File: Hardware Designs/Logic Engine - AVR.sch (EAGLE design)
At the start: 39 parts, among them IC1 MEGA328P, U1 LP2985, U2 HEX_CONVERTER, Y1 16MHz

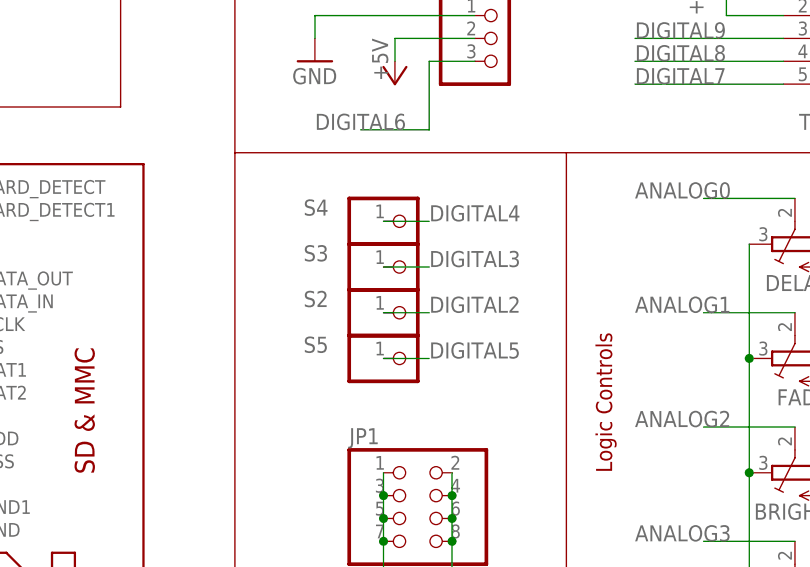
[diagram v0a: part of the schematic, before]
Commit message: Updated AVR board to production version
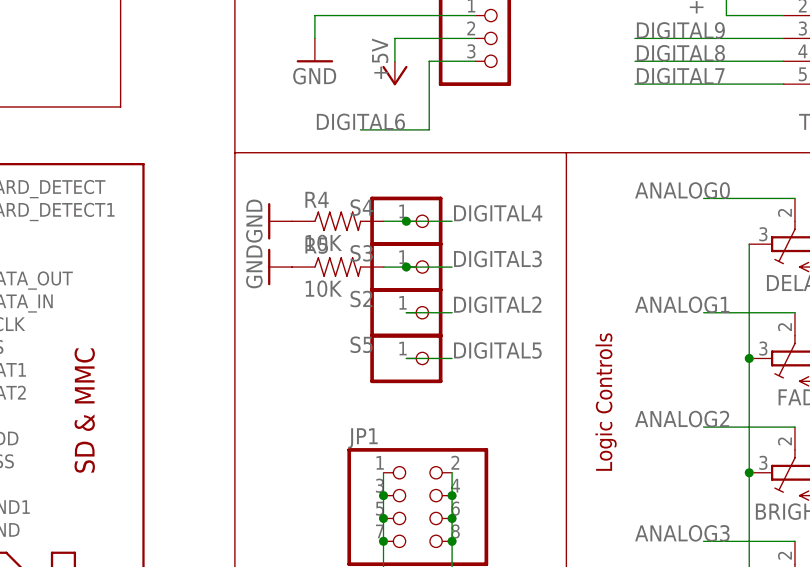
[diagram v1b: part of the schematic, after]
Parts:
- added R4, R5: 10K, SparkFun-Resistors:RESISTOR0603
- FTDI: value GRN TX RX 5V G BLK -> GRN TX RX 5V G BLK
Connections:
- net DIGITAL3: now also R5.2
- net DIGITAL4: now also R4.2
- net GND: now also R4.1, R5.1
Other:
- moved on the sheet: S2, S3, S4, S5
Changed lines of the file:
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@@
 <part name="GND11" library="supply1" deviceset="GND" device=""/>
 <part name="GND12" library="supply1" deviceset="GND" device=""/>
-<part name="FTDI" library="carduino" deviceset="PINHD-1X6" device="CLEAN" value="GRN  TX RX  5V   G  BLK"/>
+<part name="FTDI" library="carduino" deviceset="PINHD-1X6" device="CLEAN" value="GRN TX RX 5V G BLK"/>
 <part name="FRAME1" library="frames" deviceset="LETTER_L" device=""/>
 <part name="I2C" library="carduino" deviceset="PINHD-1X4" device="CB"/>
@@
 <part name="C5" library="adafruit" deviceset="CPOL-US" device="D" value="100uF"/>
 <part name="C6" library="adafruit" deviceset="C-US" device="C0805K" value="10uF"/>
+<part name="R4" library="SparkFun-Resistors" deviceset="RESISTOR" device="0603" value="10K"/>
+<part name="R5" library="SparkFun-Resistors" deviceset="RESISTOR" device="0603" value="10K"/>
+<part name="GND13" library="supply1" deviceset="GND" device=""/>
+<part name="GND14" library="supply1" deviceset="GND" device=""/>
 </parts>
 <sheets>
@@
 <instance part="R8" gate="G$1" x="106.68" y="160.02" rot="R270"/>
 <instance part="JP1" gate="A" x="190.5" y="83.82"/>
-<instance part="S4" gate="G$1" x="190.5" y="116.84" smashed="yes">
-<attribute name="NAME" x="179.07" y="117.475" size="1.778" layer="95"/>
-<attribute name="VALUE" x="184.15" y="111.76" size="1.778" layer="96"/>
-</instance>
-<instance part="S3" gate="G$1" x="190.5" y="111.76" smashed="yes">
-<attribute name="NAME" x="179.07" y="112.395" size="1.778" layer="95"/>
-<attribute name="VALUE" x="184.15" y="106.68" size="1.778" layer="96"/>
-</instance>
-<instance part="S2" gate="G$1" x="190.5" y="106.68" smashed="yes">
-<attribute name="NAME" x="179.07" y="107.315" size="1.778" layer="95"/>
-<attribute name="VALUE" x="184.15" y="101.6" size="1.778" layer="96"/>
-</instance>
-<instance part="S5" gate="G$1" x="190.5" y="101.6" smashed="yes">
-<attribute name="NAME" x="179.07" y="102.235" size="1.778" layer="95"/>
-<attribute name="VALUE" x="184.15" y="96.52" size="1.778" layer="96"/>
+<instance part="S4" gate="G$1" x="193.04" y="116.84" smashed="yes">
+<attribute name="NAME" x="184.15" y="117.475" size="1.778" layer="95"/>
+<attribute name="VALUE" x="186.69" y="111.76" size="1.778" layer="96"/>
+</instance>
+<instance part="S3" gate="G$1" x="193.04" y="111.76" smashed="yes">
+<attribute name="NAME" x="184.15" y="112.395" size="1.778" layer="95"/>
+<attribute name="VALUE" x="186.69" y="106.68" size="1.778" layer="96"/>
+</instance>
+<instance part="S2" gate="G$1" x="193.04" y="106.68" smashed="yes">
+<attribute name="NAME" x="184.15" y="107.315" size="1.778" layer="95"/>
+<attribute name="VALUE" x="186.69" y="101.6" size="1.778" layer="96"/>
+</instance>
+<instance part="S5" gate="G$1" x="193.04" y="101.6" smashed="yes">
+<attribute name="NAME" x="184.15" y="102.235" size="1.778" layer="95"/>
+<attribute name="VALUE" x="186.69" y="96.52" size="1.778" layer="96"/>
 </instance>
 <instance part="GND16" gate="1" x="195.58" y="73.66"/>
@@
 <instance part="C5" gate="G$1" x="53.34" y="165.1"/>
 <instance part="C6" gate="G$1" x="78.74" y="93.98"/>
+<instance part="R4" gate="G$1" x="182.88" y="116.84"/>
+<instance part="R5" gate="G$1" x="182.88" y="111.76"/>
+<instance part="GND13" gate="1" x="175.26" y="116.84" rot="R270"/>
+<instance part="GND14" gate="1" x="175.26" y="111.76" rot="R270"/>
 </instances>
 <busses>
@@
 <pinref part="C6" gate="G$1" pin="2"/>
 </segment>
+<segment>
+<pinref part="R4" gate="G$1" pin="1"/>
+<pinref part="GND13" gate="1" pin="GND"/>
+</segment>
+<segment>
+<pinref part="R5" gate="G$1" pin="1"/>
+<pinref part="GND14" gate="1" pin="GND"/>
+</segment>
 </net>
 <net name="N$1" class="0">
@@
 </segment>
 <segment>
-<label x="193.04" y="101.6" size="1.778" layer="95"/>
+<label x="195.58" y="101.6" size="1.778" layer="95"/>
 <pinref part="S5" gate="G$1" pin="1"/>
-<wire x1="187.96" y1="101.6" x2="193.04" y2="101.6" width="0.1524" layer="91"/>
+<wire x1="190.5" y1="101.6" x2="195.58" y2="101.6" width="0.1524" layer="91"/>
 </segment>
 </net>
@@
 </segment>
 <segment>
-<label x="193.04" y="116.84" size="1.778" layer="95"/>
+<label x="195.58" y="116.84" size="1.778" layer="95"/>
 <pinref part="S4" gate="G$1" pin="1"/>
-<wire x1="187.96" y1="116.84" x2="193.04" y2="116.84" width="0.1524" layer="91"/>
+<wire x1="190.5" y1="116.84" x2="195.58" y2="116.84" width="0.1524" layer="91"/>
+<pinref part="R4" gate="G$1" pin="2"/>
+<wire x1="187.96" y1="116.84" x2="190.5" y2="116.84" width="0.1524" layer="91"/>
+<junction x="190.5" y="116.84"/>
 </segment>
 </net>
@@
 </segment>
 <segment>
-<label x="193.04" y="111.76" size="1.778" layer="95"/>
+<label x="195.58" y="111.76" size="1.778" layer="95"/>
 <pinref part="S3" gate="G$1" pin="1"/>
-<wire x1="187.96" y1="111.76" x2="193.04" y2="111.76" width="0.1524" layer="91"/>
+<wire x1="190.5" y1="111.76" x2="195.58" y2="111.76" width="0.1524" layer="91"/>
+<pinref part="R5" gate="G$1" pin="2"/>
+<wire x1="187.96" y1="111.76" x2="190.5" y2="111.76" width="0.1524" layer="91"/>
+<junction x="190.5" y="111.76"/>
 </segment>
 </net>
@@
 </segment>
 <segment>
-<label x="193.04" y="106.68" size="1.778" layer="95"/>
+<label x="195.58" y="106.68" size="1.778" layer="95"/>
 <pinref part="S2" gate="G$1" pin="1"/>
-<wire x1="187.96" y1="106.68" x2="193.04" y2="106.68" width="0.1524" layer="91"/>
-</segment>
-</net>
+<wire x1="190.5" y1="106.68" x2="195.58" y2="106.68" width="0.1524" layer="91"/>
+</segment>
+</net>

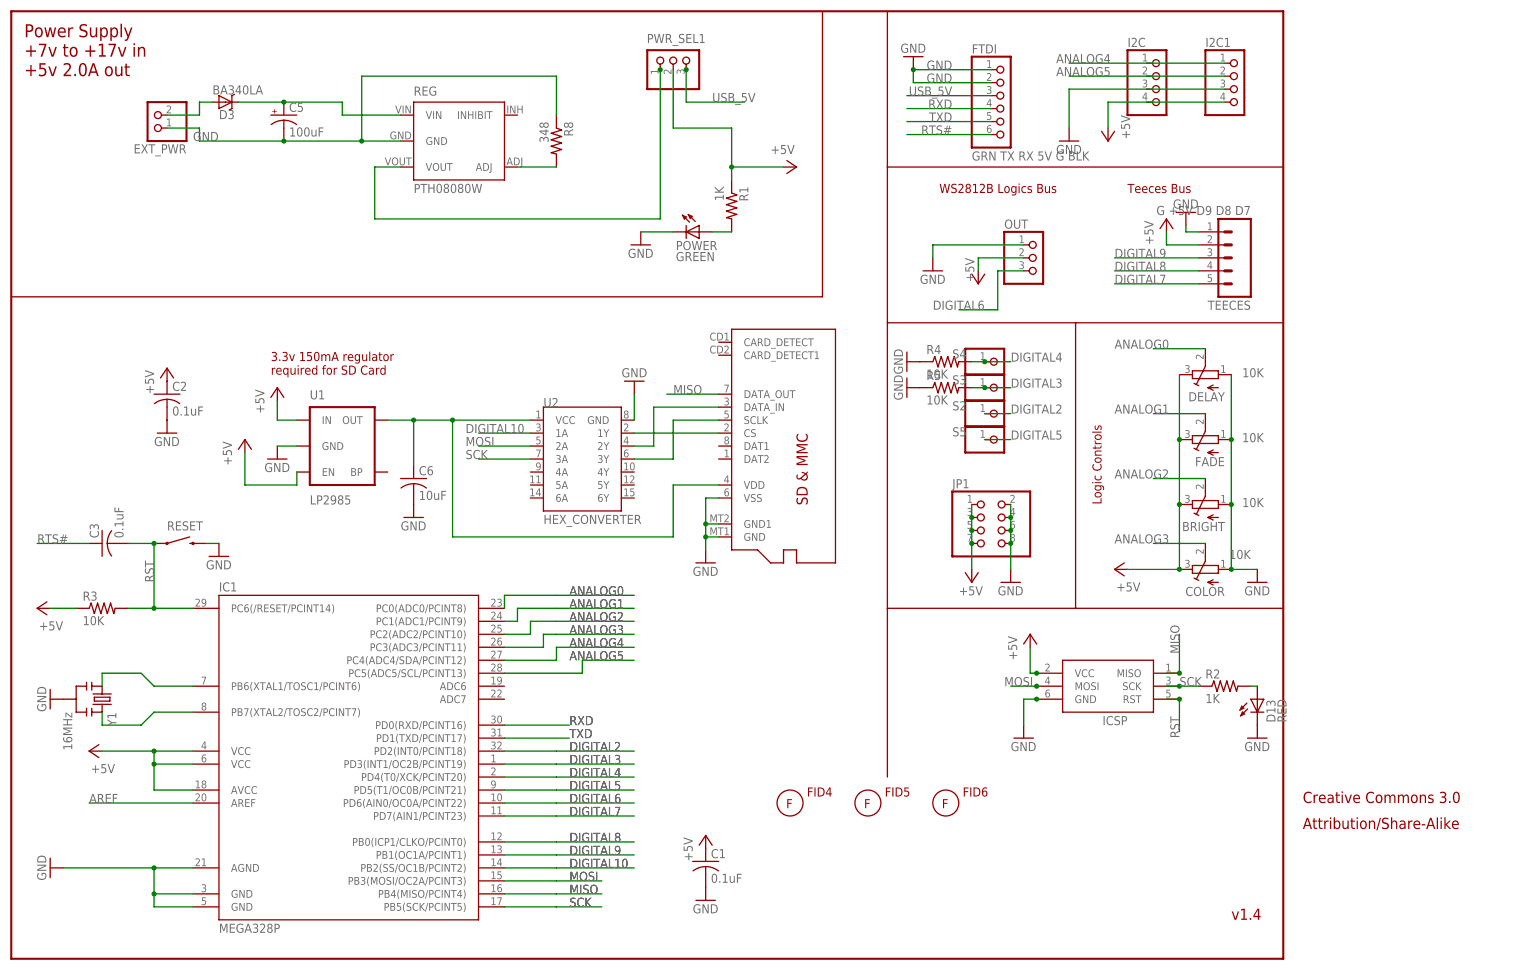
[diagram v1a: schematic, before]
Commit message: Updated AVR board slightly
Small revision to AVR board for late 2015 run (first change since these
boards were first run). Added resistor on LED output, removed reset
switch, removed 'power' jumper, moved stuff around, routed a little
smarter (I think), added fancy silkscreen art. Functionality-wise this
is identical to the previous version.
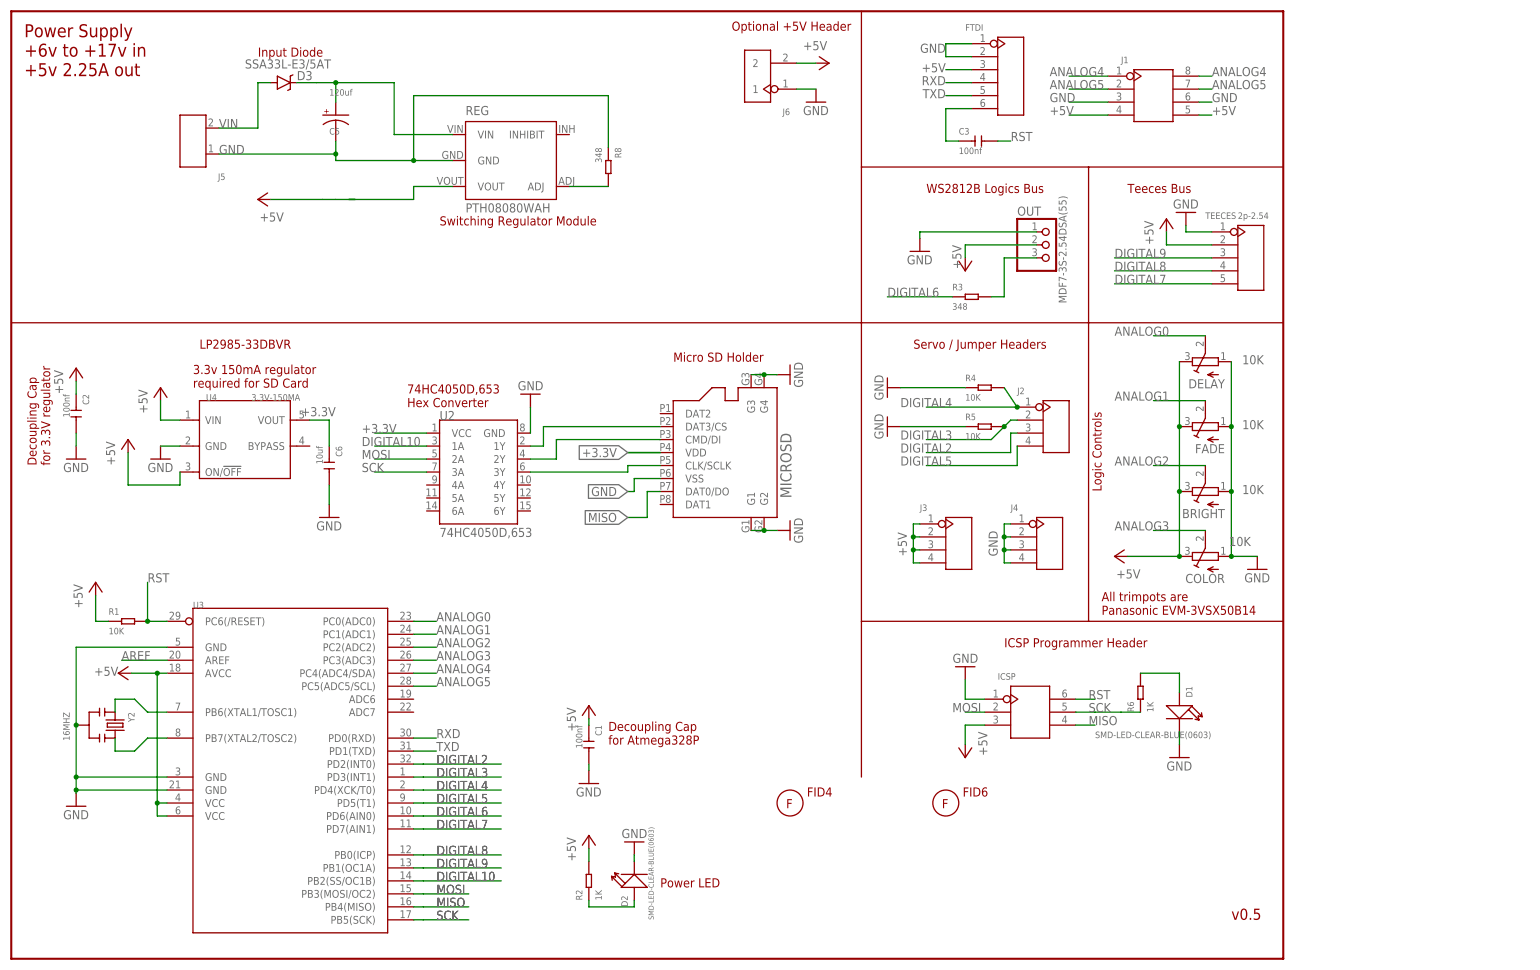
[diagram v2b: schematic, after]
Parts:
- removed D13: RED, adafruit:LEDCHIPLED_0805
- removed EXT_PWR: (no value), pinhead:PINHD-1X2
- removed FID5: (no value), SmallBatchLibPre1:FIDUCIAL
- removed I2C, I2C1: (no value), carduino:PINHD-1X4CB
- removed IC1: MEGA328P, avr-7:MEGA48/88/168-AU
- removed JP1: (no value), adafruit:PINHD-2X4
- removed POWER: GREEN, adafruit:LEDCHIPLED_0805
- removed PWR_SEL1: (no value), pinhead:PINHD-1X3
- removed RESET: RST, SparkFun-Electromechanical:SWITCH-MOMENTARY-2SMD
- removed S2, S3, S4, S5: (no value), adafruit:PINHD-1X1
- removed U1: LP2985, SparkFun-PowerIC:V_REG_LDOSMD
- removed Y1: 16MHz, SparkFun-FreqCtrl:RESONATOR16MHZ
- added D1, D2: SMD-LED-CLEAR-BLUE(0603), OPL-Diode:SMD-LED-CLEAR-BLUE(0603)
- added J1: (no value), OPL-Connector:DIP-BLACK-MALE-HEADER-VERT(2X4P-2.54)
- added J2, J3, J4: (no value), OPL-Connector:DIP-BLACK-MALE-HEADER-VERT(4P-2.54)
- added J5: (no value), OPL-Connector:SCREW-TERMINAL-GREEN(2P-3.5)
- added J6: (no value), OPL-Connector:DIP-BLACK-MALE-HEADER-VERT(2P-2.54)
- added R6: 1K, OPL-Resistor:RES-0603
- added U3: (no value), Seeed-OPL-ic:MCU-ATMEGA328P-AU(TQFP32)
- added U4: 3.3V-150MA, Seeed-OPL-ic:PMIC-LP2985-50DBVR(SOT23-5)
- added Y2: 16MHZ, Seeed-OPL-crystal-osctllator:SMD-RESONATOR-16MHZ-15PF-0.5%-40R(3P-3.2X1.3MM)
- C1, C2, C3: value 0.1uF -> 100nf; device adafruit:C-USC0805K -> Seeed-OPL-Capacitor:CERAMIC-100NF-50V-10%-X7R(0805)
- C5: value 100uF -> 120uf; device adafruit:CPOL-USD -> rseries:CPOL-USD
- C6: value 10uF -> 10uf; device adafruit:C-USC0805K -> Seeed-OPL-Capacitor:CERAMIC-10UF-25V-10%-X5R(0805)
- D3: value BA340LA -> SSA33L-E3/5AT
- FTDI: value GRN TX RX 5V G BLK -> (none); device carduino:PINHD-1X6CLEAN -> Seeed-OPL-Connector:DIP-BLACK-MALE-HEADER(6P-2.54)
- ICSP: value AVRISP-6 -> (none); device adafruit:AVRISP-6 -> Seeed-OPL-Connector:DIP-BLACK-MALE-HEADER(2X3P-2.54）-2.54
- MICROSD: value MICROSD -> MICROSD47579-001; device rseries:MICROSD -> rseries:MICROSD47579-001
- OUT: value (none) -> MDF7-3S-2.54DSA(55)
- R1: value 1K -> 10K; device SparkFun-Resistors:RESISTOR0603 -> OPL-Resistor:RES-0603
- R2, R4, R5: device SparkFun-Resistors:RESISTOR0603 -> OPL-Resistor:RES-0603
- R3: value 10K -> 348; device SparkFun-Resistors:RESISTOR0603 -> Seeed-OPL-Resistor:RES-0603
- R8: device SparkFun-Resistors:RESISTOR0603 -> Seeed-OPL-Resistor:RES-0603
- REG: value PTH08080W -> PTH08080WAH
- TEECES: value G +5V D9 D8 D7 -> 2p-2.54; device SparkFun-Connectors:M05PTH -> Seeed-OPL-Connector:DIP-BLACK-MALE-HEADER-VERT(5P-2.54)
- U2: value HEX_CONVERTER -> 74HC4050D,653
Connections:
- removed net N$1: IC1.PB6(XTAL1/TOSC1/PCINT6), Y1.1
- removed net N$11: D3.A, EXT_PWR.2
- removed net N$16: MICROSD.DATA_IN, U2.2Y
- removed net N$17: MICROSD.SCLK, U2.3Y
- removed net N$18: MICROSD.CS, U2.1Y
- removed net N$2: IC1.PB7(XTAL2/TOSC2/PCINT7), Y1.3
- removed net N$21: PWR_SEL1.1, REG.VOUT
- removed net USB_5V: FTDI.3, PWR_SEL1.3
- removed net VDD: C6.1, MICROSD.VDD, U1.OUT, U2.VCC
- new net +3.3V: C6.1, MICROSD.VDD, U2.VCC, U4.VOUT
- new net CS: MICROSD.DAT3/CS, U2.1Y
- new net DATA_IN: MICROSD.CMD/DI, U2.2Y
- new net N$10: U3.PB7(XTAL2/TOSC2), Y2.3
- new net N$7: OUT.3, R3.2
- new net N$9: U3.PB6(XTAL1/TOSC1), Y2.1
- new net SCLK: MICROSD.CLK/SCLK, U2.3Y
- new net VIN: D3.A, J5.2
- net +5V: now also FTDI.3, ICSP.3, J1.4, J1.5, J3.P$1, J3.P$2, J3.P$3, J3.P$4, J6.2, R2.2, REG.VOUT, U3.AVCC, U3.VCC@1, U3.VCC@2, U4.ON/!OFF, U4.VIN; no longer I2C.4, I2C1.4, IC1.AVCC, IC1.VCC@1, IC1.VCC@2, ICSP.VCC, JP1.1, JP1.3, JP1.5, JP1.7, PWR_SEL1.2, R3.1, U1.EN, U1.IN
- net ANALOG0: now also U3.PC0(ADC0); no longer IC1.PC0(ADC0/PCINT8)
- net ANALOG1: now also U3.PC1(ADC1); no longer IC1.PC1(ADC1/PCINT9)
- net ANALOG2: now also U3.PC2(ADC2); no longer IC1.PC2(ADC2/PCINT10)
- net ANALOG3: now also U3.PC3(ADC3); no longer IC1.PC3(ADC3/PCINT11)
- net ANALOG4: now also J1.1, J1.8, U3.PC4(ADC4/SDA); no longer I2C.1, I2C1.1, IC1.PC4(ADC4/SDA/PCINT12)
- net ANALOG5: now also J1.2, J1.7, U3.PC5(ADC5/SCL); no longer I2C.2, I2C1.2, IC1.PC5(ADC5/SCL/PCINT13)
- net AREF: now also U3.AREF; no longer IC1.AREF
- net DIGITAL10: now also U3.PB2(SS/OC1B); no longer IC1.PB2(SS/OC1B/PCINT2)
- net DIGITAL2: now also J2.P$3, U3.PD2(INT0); no longer IC1.PD2(INT0/PCINT18), S2.1
- net DIGITAL3: now also J2.P$2, U3.PD3(INT1); no longer IC1.PD3(INT1/OC2B/PCINT19), S3.1
- net DIGITAL4: now also J2.P$1, U3.PD4(XCK/T0); no longer IC1.PD4(T0/XCK/PCINT20), S4.1
- net DIGITAL5: now also J2.P$4, U3.PD5(T1); no longer IC1.PD5(T1/OC0B/PCINT21), S5.1
- net DIGITAL6: now also R3.1, U3.PD6(AIN0); no longer IC1.PD6(AIN0/OC0A/PCINT22), OUT.3
- net DIGITAL7: now also U3.PD7(AIN1); no longer IC1.PD7(AIN1/PCINT23)
- net DIGITAL8: now also U3.PB0(ICP); no longer IC1.PB0(ICP1/CLKO/PCINT0)
- net DIGITAL9: now also U3.PB1(OC1A); no longer IC1.PB1(OC1A/PCINT1)
- net GND: now also D1.-, D2.-, ICSP.1, J1.3, J1.6, J4.P$1, J4.P$2, J4.P$3, J4.P$4, J5.1, J6.1, MICROSD.G1, MICROSD.G2, MICROSD.G3, MICROSD.G4, U3.GND, U3.GND@1, U3.GND@2, U4.GND, Y2.2; no longer D13.C, EXT_PWR.1, I2C.3, I2C1.3, IC1.AGND, IC1.GND@1, IC1.GND@2, ICSP.GND, JP1.2, JP1.4, JP1.6, JP1.8, MICROSD.GND, MICROSD.GND1, POWER.C, RESET.2, U1.GND, Y1.2
- net MISO: now also ICSP.4, MICROSD.DAT0/DO, U3.PB4(MISO); no longer IC1.PB4(MISO/PCINT4), ICSP.MISO, MICROSD.DATA_OUT
- net MOSI: now also ICSP.2, U3.PB3(MOSI/OC2); no longer IC1.PB3(MOSI/OC2A/PCINT3), ICSP.MOSI
- net N$4: now also D1.+, R6.2; no longer D13.A, R2.2
- net N$5: now also D2.+, R2.1; no longer POWER.A, R1.2
- net RST: now also ICSP.6, R1.2, U3.PC6(/RESET); no longer IC1.PC6(/RESET/PCINT14), ICSP.RST, R3.2, RESET.1
- net RXD: now also U3.PD0(RXD); no longer IC1.PD0(RXD/PCINT16)
- net SCK: now also ICSP.5, R6.1, U3.PB5(SCK); no longer IC1.PB5(SCK/PCINT5), ICSP.SCK, R2.1
- net TXD: now also U3.PD1(TXD); no longer IC1.PD1(TXD/PCINT17)
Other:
- note added: "74HC4050D,653 Hex Converter"
- note added: "All trimpots are Panasonic EVM‑3VSX50B14"
- note added: "Decoupling Cap for 3.3V regulator"
- note added: "Decoupling Cap for Atmega328P"
- note added: "ICSP Programmer Header"
- note added: "Input Diode"
- note added: "LP2985-33DBVR"
- note added: "Micro SD Holder"
- note added: "Optional +5V Header"
- note added: "Power LED"
- note added: "Power Supply +6v to +17v in +5v 2.25A out"
- note added: "Servo / Jumper Headers"
- note added: "Switching Regulator Module"
- note added: "v0.5"
- note removed: "Attribution/Share-Alike"
- note removed: "Creative Commons 3.0"
- note removed: "Power Supply +7v to +17v in +5v 2.0A out"
- note removed: "v1.4"
- moved on the sheet: BRIGHT, C5, COLOR, DELAY, FADE, OUT, REG, U2
